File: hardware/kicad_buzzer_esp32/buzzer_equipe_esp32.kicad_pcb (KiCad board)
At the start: 2 copper layers, 70 x 103 mm, 7 parts, among them J2 Module charge TP4056+protect+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, J3 Module vibreur IN/VCC/GND - C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, SW1 Bouton BUZZ (fils volants) - 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, SW2 Interrupteur marche/arret (fi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, U1L ESP32 colonne gauche (broches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, U1R ESP32 colonne droite (broches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

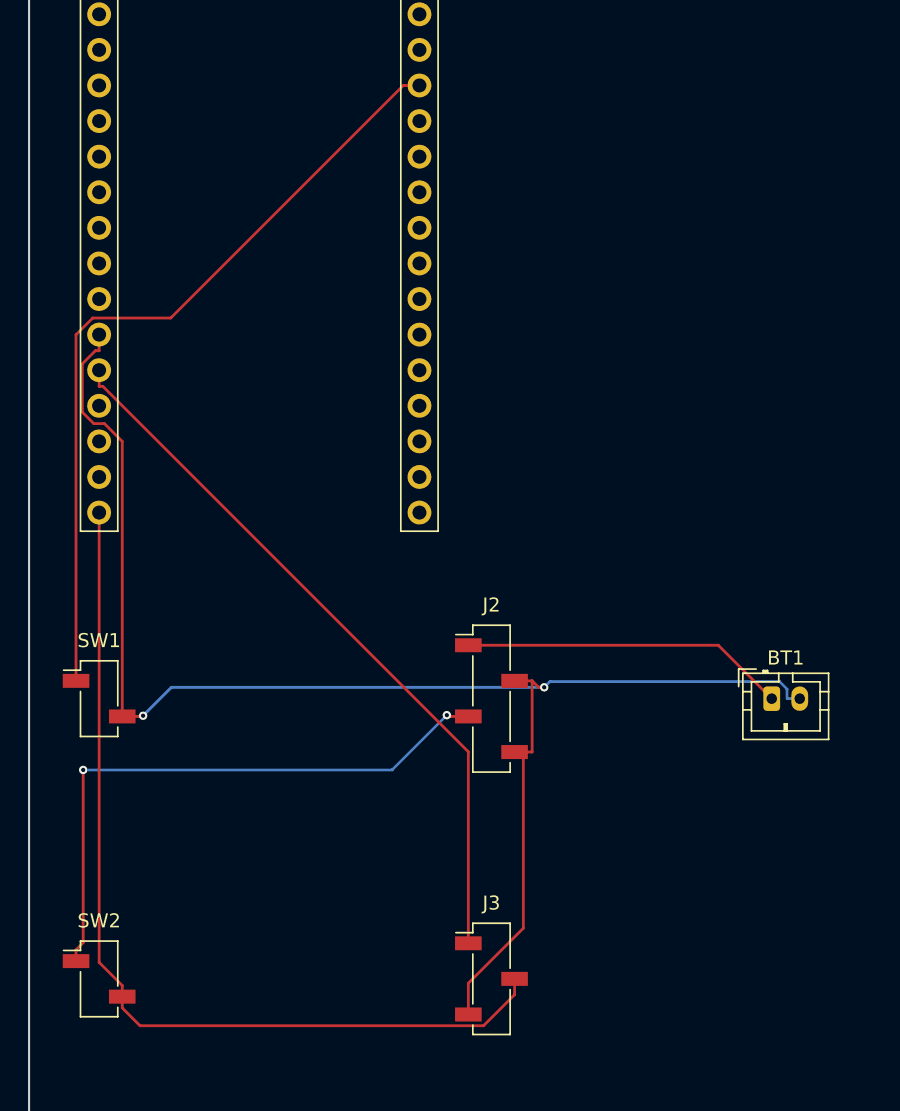
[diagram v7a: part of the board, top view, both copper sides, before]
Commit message: hardware: ajoute BATLED, indicateur de niveau de batterie (4 LED)
Le client revient sur la decision precedente (pas de LED, juste la coupure
protectrice) et demande un indicateur de niveau de batterie. Ajoute un
connecteur BATLED (2 broches CMS) sur les cartes Nano et ESP32, branche
directement en parallele sur la batterie (meme net que BT1 : broche 1=B+,
broche 2=B-).

Module cible verifie via handsontec.com: "1S lithium battery capacity
indicator", 2 fils seulement (pas de VCC/GND separe, pas de bouton --
toujours actif, ~5mA), 4 LED montrant 25/50/75/100%. BOM mis a jour
(docs/BOM_BUZZER_EQUIPE.md).

Les 2 cartes re-routees (Freerouting) et revalidees (kicad-cli pcb drc):
0 violation de clearance, 0 element non connecte, keepout nRF24 (nano)
toujours respecte, 0 track_dangling apres nettoyage des residus habituels.

Co-Authored-By: Claude Sonnet 5 <noreply@anthropic.com>
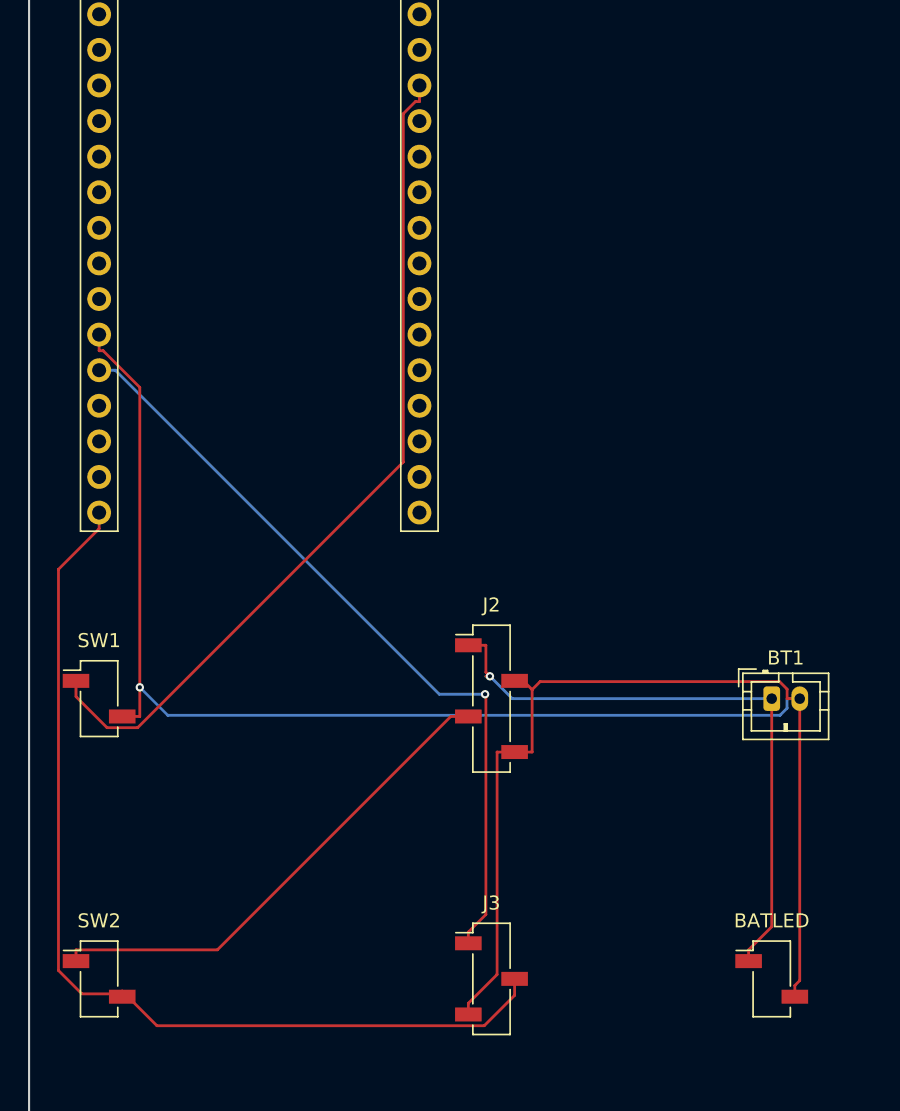
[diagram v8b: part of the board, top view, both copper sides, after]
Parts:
- added BATLED: Indicateur niveau batterie (4 LED) - CMS - 1=B+ 2=B-, Connector_PinSocket_2.54mm:PinSocket_1x02_P2.54mm_Vertical_SMD_Pin1Left, F.Cu at (58.0, 95.0)
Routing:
- net GND: track 108.8 -> 148.4 mm, vias 2 -> 1
- net BAT_PLUS: track 23.2 -> 44.3 mm, vias 0 -> 1
- net VCC_5V_RAW: track 43.1 -> 35.7 mm, vias 2 -> 0
- net BTN_SIG: track 56.6 -> 60.8 mm
- net VCC_5V_SW: track 66.6 -> 70.6 mm
- net VIBE_IN: track 52.0 -> 55.4 mm, vias 0 -> 1
